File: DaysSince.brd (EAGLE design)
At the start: 85.1 x 55.9 mm, 3 parts

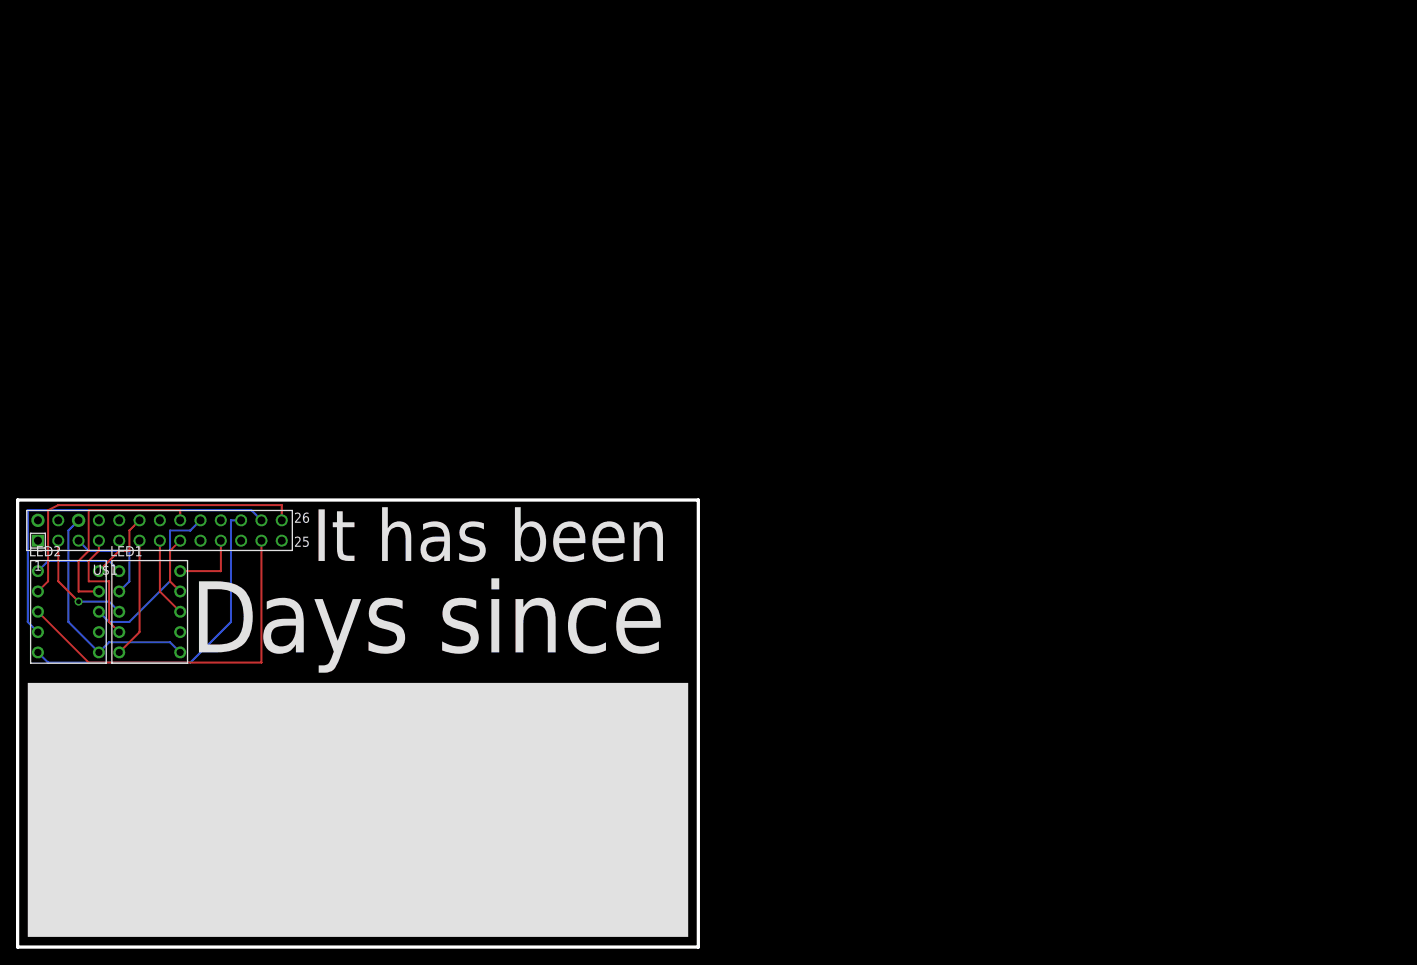
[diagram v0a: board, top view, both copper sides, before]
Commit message: New and improved version
Smaller PCB, shift registers, and lower cost, woo.
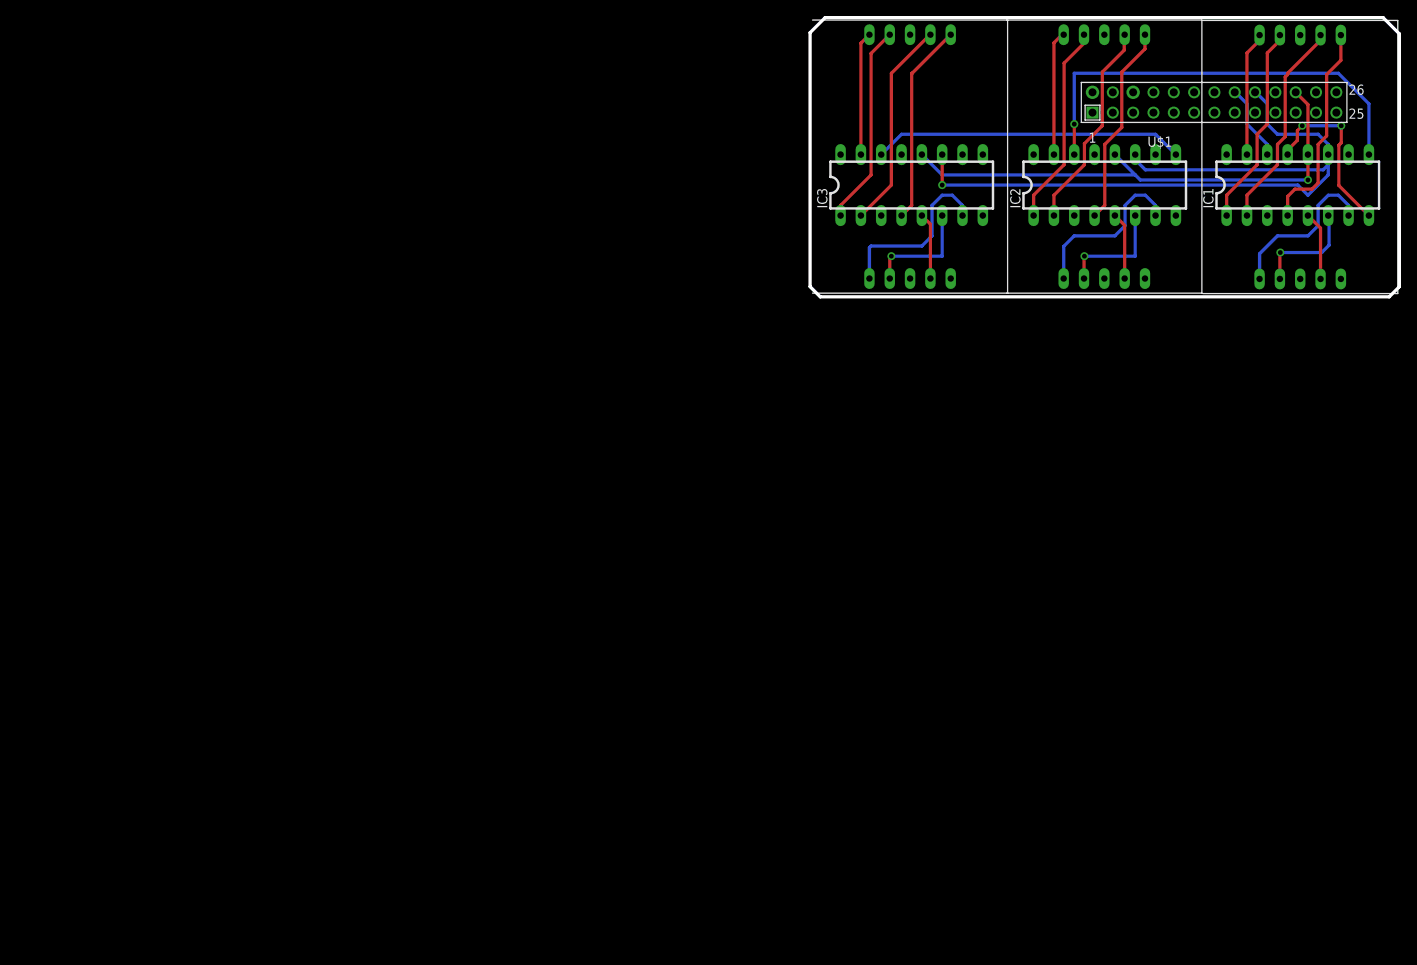
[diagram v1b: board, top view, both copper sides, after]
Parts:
- added IC1, IC2, IC3: 74LS595N, SparkFun-DigitalIC:DIL16
- added LED3: 7SG100012AG, Benchoff:7SG100012AG
- LED1, LED2: value LA-401AN -> 7SG100012AG; device led-7-segment:LA-401 -> Benchoff:7SG100012AG
- moved LED1 154.6 mm to (161.6, 100.0)
- moved U$1 142.3 mm to (135.6, 105.6)
- moved LED2 141.4 mm to (137.1, 100.1)
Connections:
- new net 5V: IC1.10, IC1.16, IC2.10, IC2.16, IC3.10, IC3.16, U$1.2
- new net N$1: IC1.9, IC2.14
- new net N$10: IC1.6, LED1.2
- new net N$17: IC2.6, LED2.2
- new net N$18: IC2.5, LED2.4
- new net N$19: IC2.15, LED2.10
- new net N$20: IC3.7, LED3.1
- new net N$21: IC3.6, LED3.2
- new net N$22: IC3.5, LED3.4
- new net N$23: IC3.4, LED3.6
- new net N$24: IC3.2, LED3.7
- new net N$25: IC3.1, LED3.9
- new net N$26: IC3.15, LED3.10
- net GND: now also IC1.13, IC1.8, IC2.13, IC2.8, IC3.13, IC3.8, LED1.3, LED1.8, LED2.3, LED2.8, LED3.3, LED3.8; no longer LED1.1, LED1.6, LED2.1, LED2.6
- net N$11: now also IC1.5, LED1.4; no longer LED2.9, U$1.16
- net N$12: now also IC1.4, LED1.6; no longer LED2.8, U$1.18
- net N$13: now also IC1.2, LED1.7; no longer LED2.5, U$1.22
- net N$14: now also IC1.1, LED1.9; no longer LED2.4, U$1.24
- net N$15: now also IC1.15, LED1.10; no longer LED2.2, U$1.26
- net N$16: now also IC2.7, LED2.1; no longer LED2.3, U$1.23
- net N$2: now also IC2.9, IC3.14; no longer LED1.3, U$1.3
- net N$3: now also IC2.4, LED2.6; no longer LED2.10, U$1.12
- net N$4: now also IC1.12, IC2.12, IC3.12, U$1.22; no longer LED1.2, U$1.5
- net N$5: now also IC1.11, IC2.11, IC3.11, U$1.18; no longer LED1.4, U$1.7
- net N$6: now also IC1.14, U$1.16; no longer LED1.5, U$1.11
- net N$7: now also IC2.2, LED2.7; no longer LED1.8, U$1.13
- net N$8: now also IC2.1, LED2.9; no longer LED1.9, U$1.15
- net N$9: now also IC1.7, LED1.1; no longer LED1.10, U$1.19
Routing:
- net N$5: track 15.0 -> 96.3 mm, vias 0 -> 1
- net N$1: track 0.00 -> 54.9 mm, vias 0 -> 1
- net N$4: track 12.5 -> 64.8 mm, vias 0 -> 1
- net N$15: track 42.0 -> 15.6 mm
- net N$24: track 0.00 -> 26.2 mm
- net N$23: track 0.00 -> 25.2 mm
- net N$25: track 0.00 -> 25.2 mm
- net N$2: track 14.3 -> 38.9 mm, vias 1 -> 0
- net N$16: track 45.8 -> 21.4 mm
- net N$20: track 0.00 -> 22.2 mm
- net N$14: track 45.5 -> 25.3 mm
- net GND: track 41.0 -> 22.2 mm, vias 0 -> 2
- net N$8: track 7.40 -> 25.2 mm
- net N$11: track 25.9 -> 8.58 mm
- net N$7: track 9.94 -> 26.3 mm
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- added copper zone on layer 1, net 5V
- removed copper zone on layer 1, net N$1
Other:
- board size 85.1 x 55.9 mm -> 73.7 x 34.9 mm
- board text removed: "Days since"
- board text removed: "It has been"

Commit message: Updated for shift registers
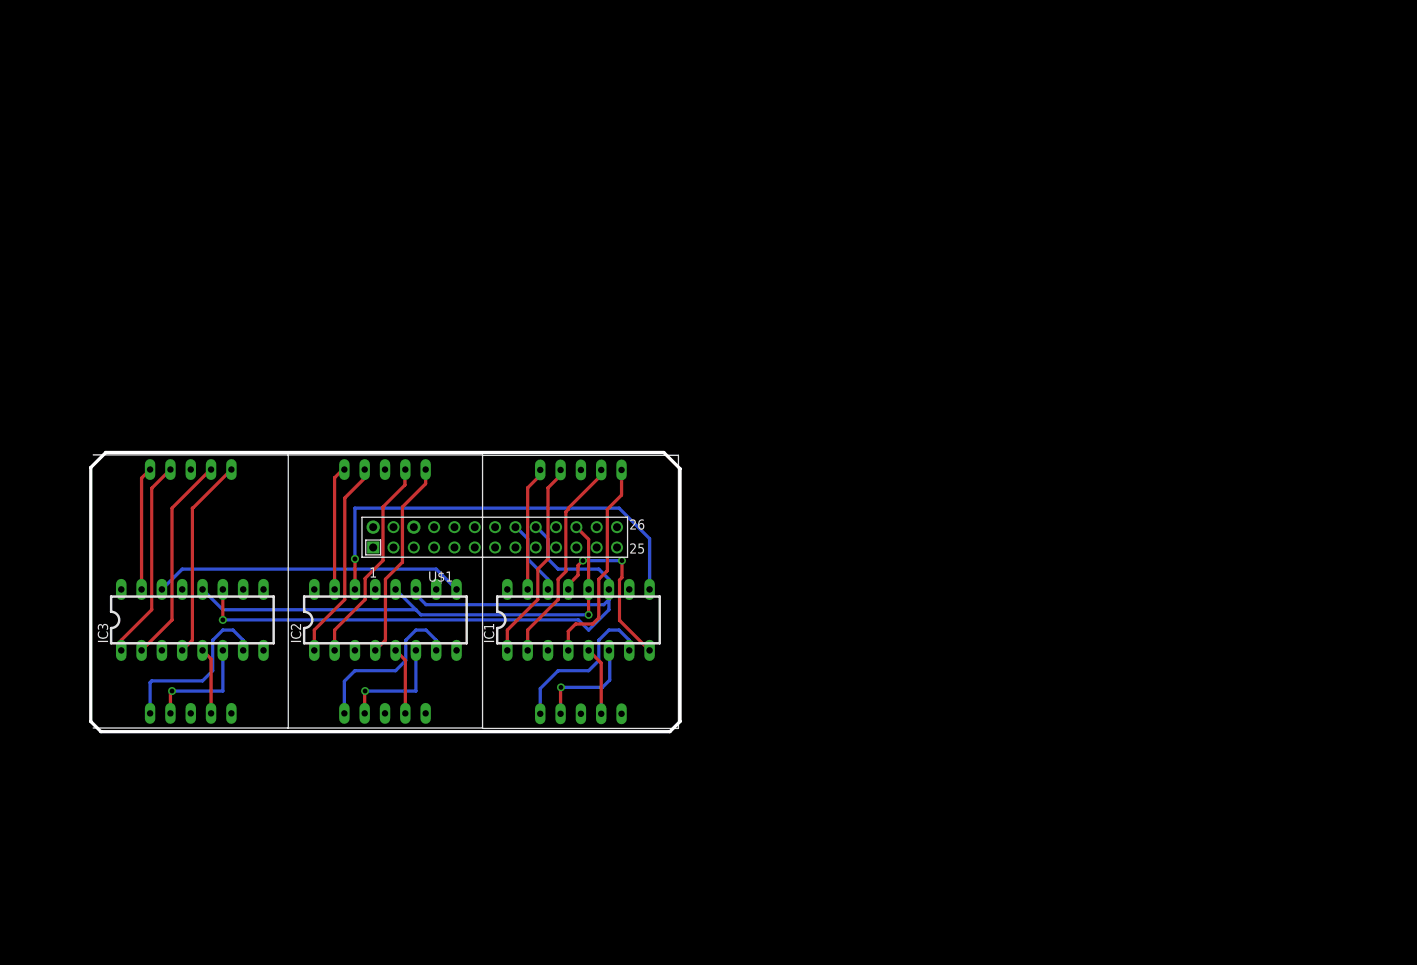
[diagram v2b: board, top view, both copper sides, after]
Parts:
- moved LED3 105.1 mm to (22.9, 45.7)
- moved IC1 105.1 mm to (71.4, 42.2)
- moved IC2 105.1 mm to (47.2, 42.2)
- moved IC3 105.1 mm to (23.1, 42.2)
- moved LED1 105.1 mm to (71.7, 45.7)
- moved LED2 105.1 mm to (47.2, 45.7)
- moved U$1 105.1 mm to (45.7, 51.2)
